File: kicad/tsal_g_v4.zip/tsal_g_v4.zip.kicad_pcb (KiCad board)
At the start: 2 copper layers, 115 x 60 mm, 90 parts, among them J1 Conn_01x02_Pin, J2 Conn_01x02_Pin, J3 Conn_01x06_Pin, J6 Conn_01x02_Pin, J7 Conn_01x02_Pin, J8 Conn_01x03, Q1 2N7002, Q4 QM6015D, U1 TL431DBZ, U10 BU4S01G2, U11 BU4S01G2, U12 4077, U13 BU4S71G2, U14 BUS4S71G2, U16 BU4SU69G2, U2 LTV-817S, U20 4071, U3 B1212, U4 BU4SU69G2, U5 40106, U6 40106, U7 BU4S81G2, U9 40106

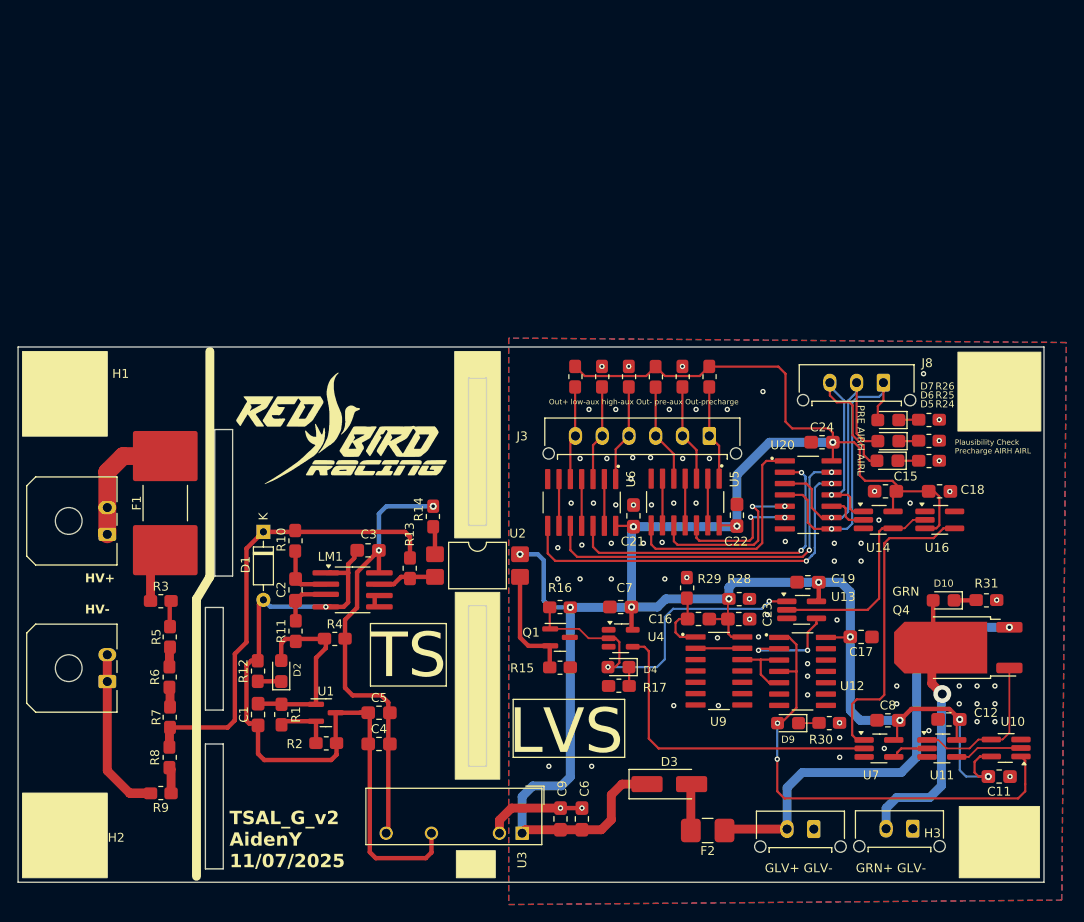
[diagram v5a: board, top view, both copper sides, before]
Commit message: Updated plausibility latch logic
need review
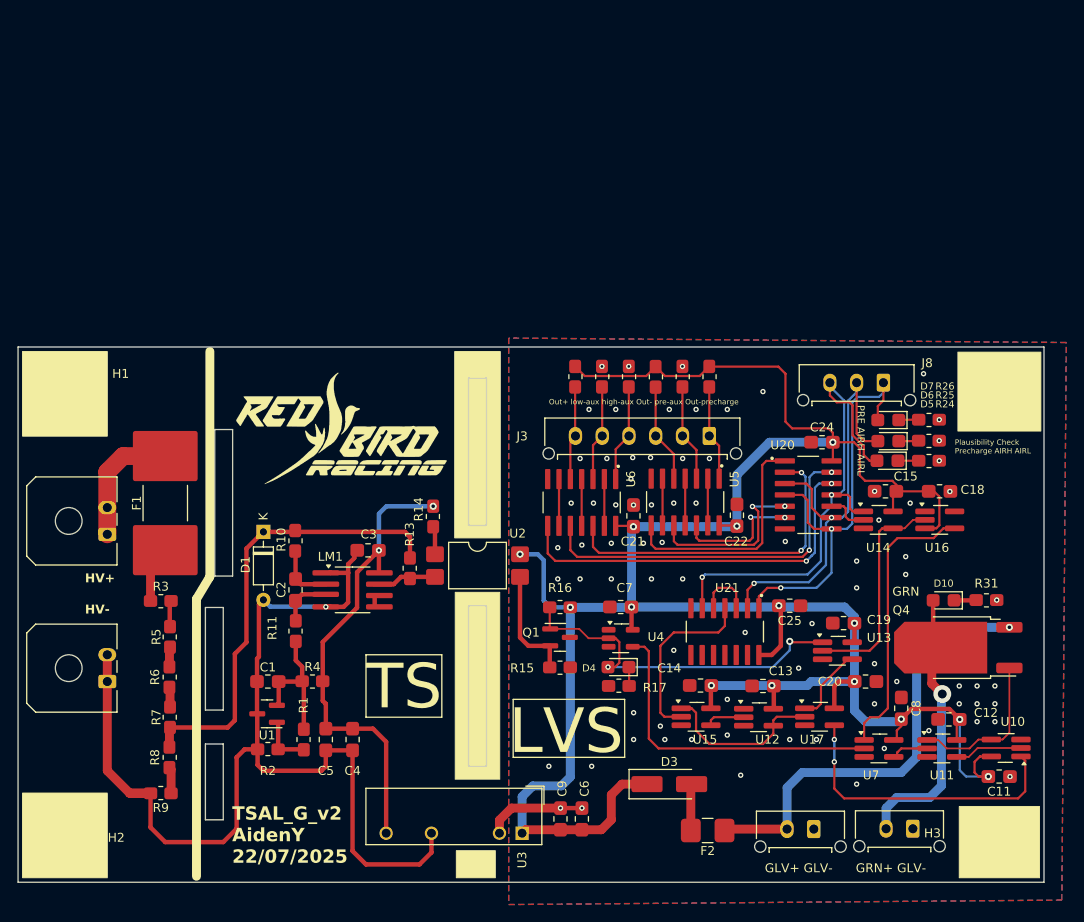
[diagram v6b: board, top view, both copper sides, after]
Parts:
- removed C16, C17, C23: 0.1uF, RMC_Capacitor:C_0805_2012Metric_Pad1.18x1.45mm_HandSolder_L
- removed D2, D9: LED, RMC_LED:LED_0805_2012Metric_Pad1.45x1.40mm_HandSolder
- removed R12, R30: 1k, RMC_Resistor:R_0805_2012Metric_Pad1.20x1.40mm_HandSolder_L
- removed R28: 10k, RMC_Resistor:R_0805_2012Metric_Pad1.20x1.40mm_HandSolder_L
- removed R29: 100k, RMC_Resistor:R_0805_2012Metric_Pad1.20x1.40mm_HandSolder_L
- removed U9: 40106, RMC_SO:SOIC127P600X175-14N
- added C13: 0.1uF, RMC_Capacitor:C_0805_2012Metric_Pad1.18x1.45mm_HandSolder_L, F.Cu at (140.0, 91.0)
- added C14: 0.1uF, RMC_Capacitor:C_0805_2012Metric_Pad1.18x1.45mm_HandSolder_L, F.Cu at (133.0, 91.0)
- added C20: 0.1uF, RMC_Capacitor:C_0805_2012Metric_Pad1.18x1.45mm_HandSolder_L, F.Cu at (151.5, 90.5)
- added C25: 0.1uF, RMC_Capacitor:C_0805_2012Metric_Pad1.18x1.45mm_HandSolder_L, F.Cu at (143.0, 82.0)
- added U15: BU4S01G2, RMC_SOT:SOT-23-5_HandSoldering_Extended_RMC, F.Cu at (132.5, 94.5)
- added U17: BU4S71G2, RMC_SOT:SOT-23-5_HandSoldering_Extended_RMC, F.Cu at (146.3, 94.5)
- added U21: 4071, RMC_SO:SOIC127P600X175-14N, F.Cu at (135.7, 84.9)
- U12: value 4077 -> BU4S01G2; footprint RMC_SO:SOIC127P600X175-14N -> RMC_SOT:SOT-23-5_HandSoldering_Extended_RMC
- moved U12 7.12 mm to (139.5, 94.5)
- moved C5 6.67 mm to (91.0, 97.0), turned to 90 degrees
- moved U1 6.59 mm to (84.4, 94.1), turned to 180 degrees
- moved R2 6.58 mm to (84.5, 98.1), turned to 180 degrees
- moved C19 6.09 mm to (149.0, 84.0)
- moved U13 6.09 mm to (148.3, 87.0)
- moved R4 5.39 mm to (89.5, 90.5)
- moved C1 3.86 mm to (84.5, 90.5), turned to 180 degrees
- moved R1 3.75 mm to (88.5, 97.0)
- moved C4 3.00 mm to (94.0, 97.0), turned to 90 degrees
- moved C8 2.02 mm to (155.5, 93.5), turned to -90 degrees
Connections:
- J2 pad 1: /-HV -> GND
- J2 pad 2: /-HV -> GND
- R9 pad 2: /-HV -> GND
- U1 pad 1: /Vref -> Net-(U1-REF)
- U1 pad 2: Net-(U1-REF) -> /Vref
- U12 pad 1: RESET -> GLV-
- U12 pad 3: Net-(U12-Pad3) -> GLV-
- U12 pad 4: RESET -> Net-(U12-Pad4)
- U12 pad 5: Net-(U12-Pad3) -> VCC
- U13 pad 4: Net-(U12-Pad2) -> Net-(U13-Pad4)
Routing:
- net GND: track 81.7 -> 121.0 mm
- net AIRL Check: track 31.7 -> 57.1 mm, vias 1 -> 2
- net /-HV: track 21.4 -> 0.00 mm
- net RESET: track 54.3 -> 33.4 mm
- net Net-(U15-Pad2): track 0.00 -> 20.2 mm
- net VCC: track 260.5 -> 279.4 mm, vias 12 -> 14
- net Net-(U12-Pad4): track 0.00 -> 18.8 mm
- net AIRH Check: track 34.0 -> 51.0 mm, vias 1 -> 2
- net Precharge Check: track 36.4 -> 49.4 mm, vias 1 -> 2
- net Net-(U13-Pad4): track 0.00 -> 8.77 mm
- net Net-(U12-Pad3): track 8.26 -> 0.00 mm
- net Net-(U12-Pad2): track 11.9 -> 4.38 mm, vias 2 -> 0
- net Net-(C16-Pad2): track 7.35 -> 0.00 mm
- net Net-(U21-Pad3): track 0.00 -> 6.50 mm
- net /Vref: track 21.4 -> 15.6 mm
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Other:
- outline, holes or cut-outs redrawn
- board text added: "TSAL_G_v2 AidenY 22/07/2025"
- board text removed: "TSAL_G_v2 AidenY 11/07/2025"

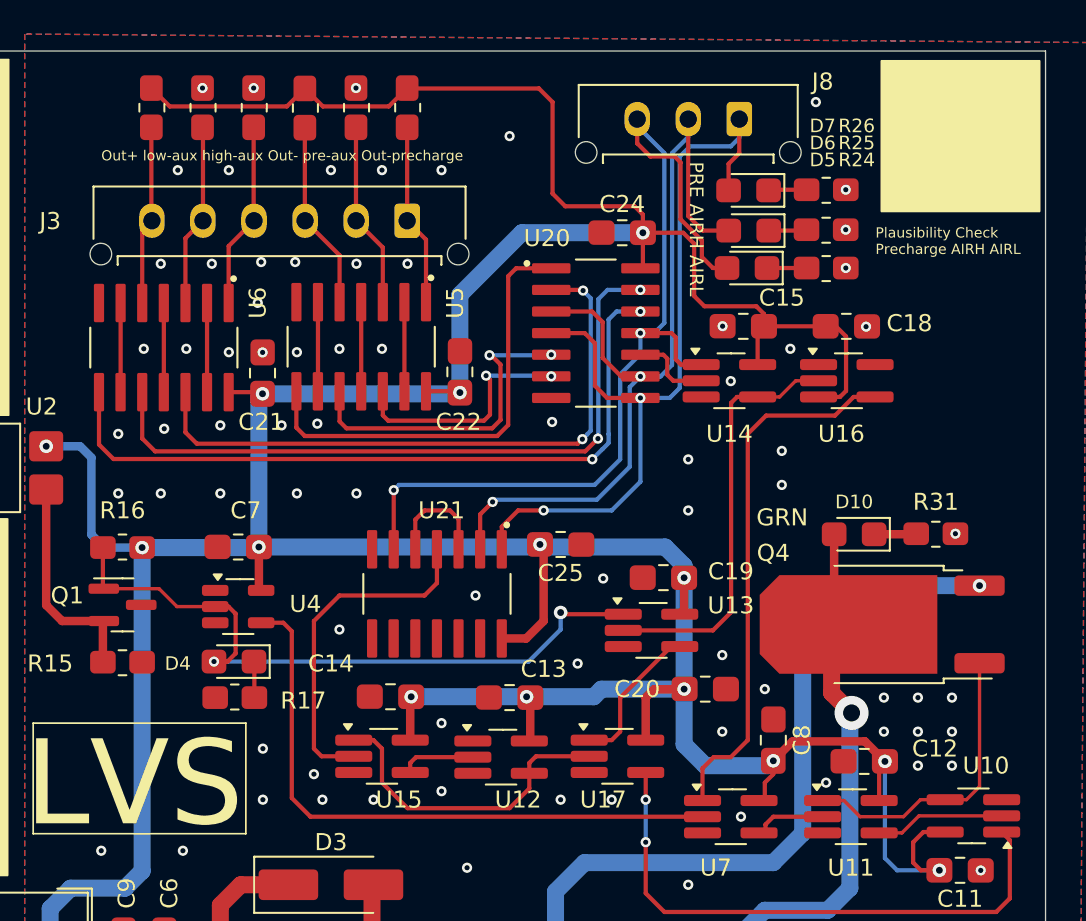
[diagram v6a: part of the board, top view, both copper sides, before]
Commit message: changes in tsal_g
silkscreen, traces
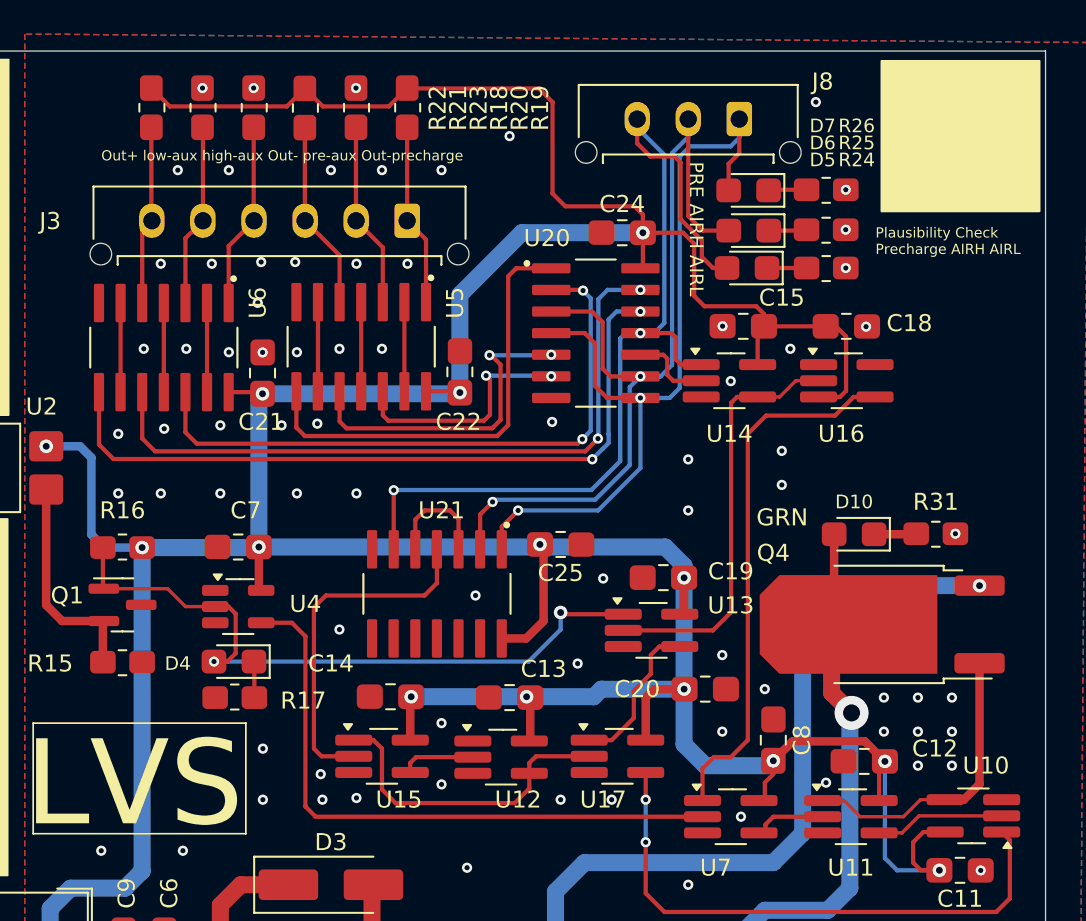
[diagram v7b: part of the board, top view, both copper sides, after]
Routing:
- net AIRL Check: track 57.1 -> 57.7 mm

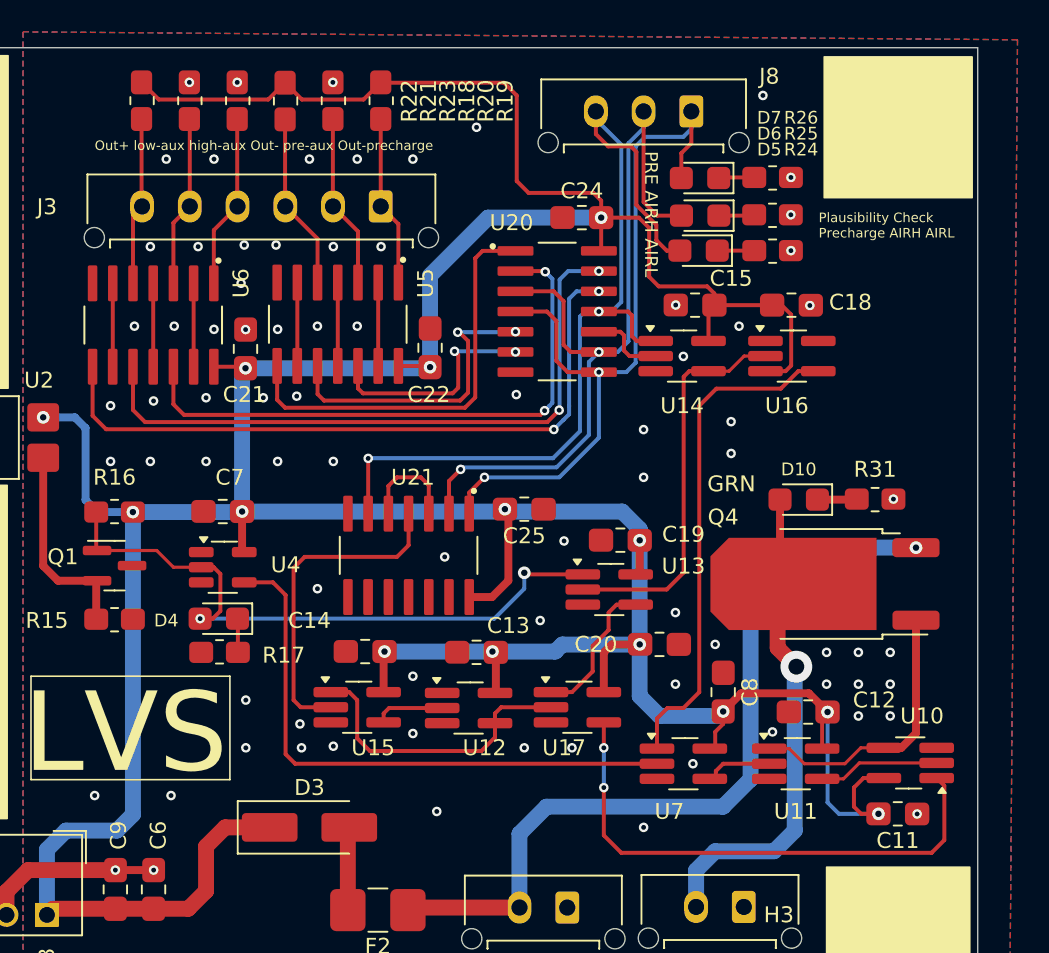
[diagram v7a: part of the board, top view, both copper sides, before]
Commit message: updated cd4001
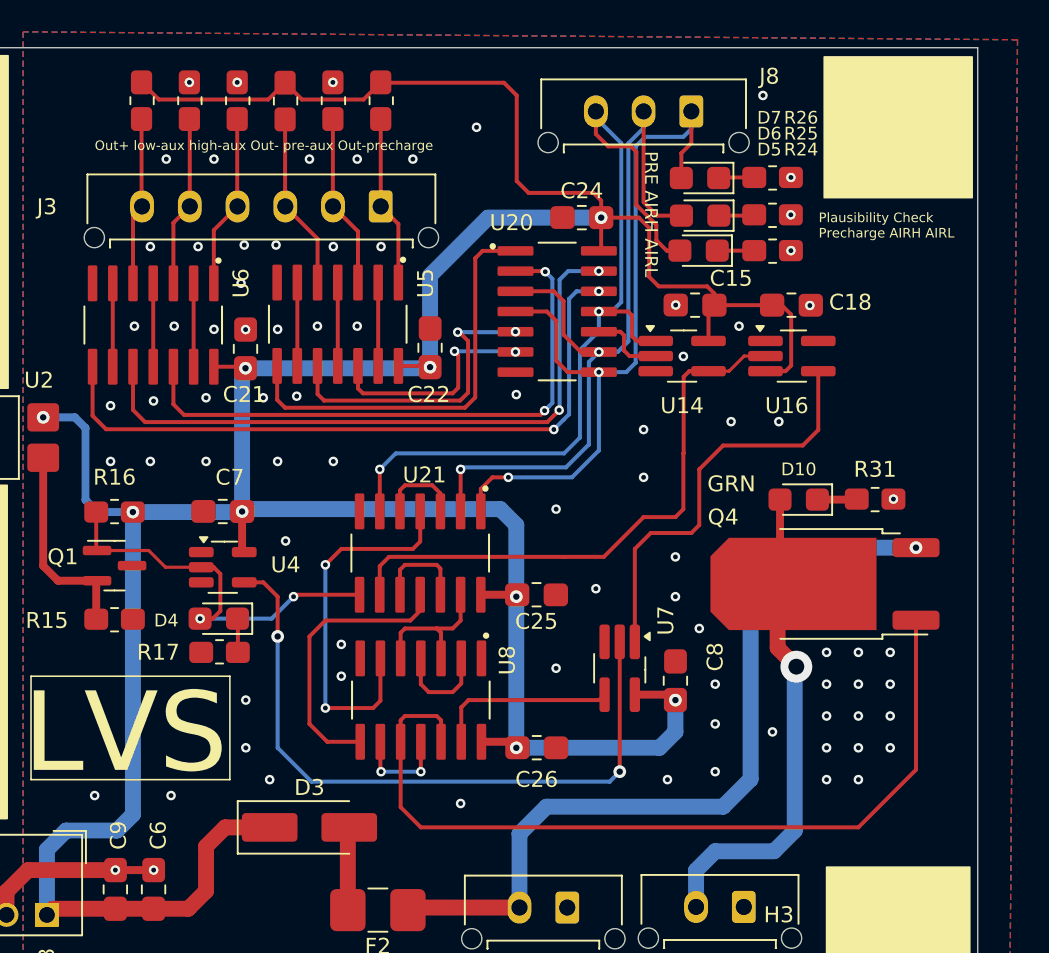
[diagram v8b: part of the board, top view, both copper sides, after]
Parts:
- removed C11, C12, C13, C14, C19, C20: 0.1uF, RMC_Capacitor:C_0805_2012Metric_Pad1.18x1.45mm_HandSolder_L
- removed U10, U11, U12, U15: BU4S01G2, RMC_SOT:SOT-23-5_HandSoldering_Extended_RMC
- removed U13, U17: BU4S71G2, RMC_SOT:SOT-23-5_HandSoldering_Extended_RMC
- added C26: 0.1uF, RMC_Capacitor:C_0805_2012Metric_Pad1.18x1.45mm_HandSolder_L, F.Cu at (143.8, 97.0)
- added U8: 4001, RMC_SO:SOIC127P600X175-14N, F.Cu at (136.5, 94.0)
- moved U7 7.21 mm to (149.0, 92.0), turned to -90 degrees
- moved C25 5.43 mm to (143.8, 87.4)
- moved C8 3.08 mm to (152.5, 92.8)
- moved U21 0.74 mm to (136.5, 84.8)
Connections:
- U21 pad 10: unconnected-(U21-Pad10) -> Net-(U21-Pad10)
- U21 pad 11: unconnected-(U21-Pad11) -> RESET
- U21 pad 12: unconnected-(U21-Pad12) -> Net-(U21-Pad10)
- U21 pad 13: unconnected-(U21-Pad13) -> Net-(U21-Pad13)
- U21 pad 8: unconnected-(U21-Pad8) -> TS RESET
- U21 pad 9: unconnected-(U21-Pad9) -> RELAY RESET
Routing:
- net VCC: track 279.4 -> 226.0 mm, vias 14 -> 9
- net Net-(Q4-G): track 17.5 -> 53.4 mm
- net Net-(U12-Pad4): track 18.8 -> 0.00 mm
- net RESET: track 33.4 -> 17.8 mm, vias 2 -> 0
- net TS RESET: track 40.5 -> 25.2 mm
- net RELAY RESET: track 24.8 -> 36.4 mm
- net Net-(U21-Pad13): track 0.00 -> 9.31 mm
- net Net-(U13-Pad4): track 9.18 -> 0.00 mm
- net Net-(U10-Pad2): track 7.61 -> 0.00 mm
- net Net-(U7-Pad4): track 4.04 -> 11.5 mm
- net Net-(U8-Pad11): track 0.00 -> 6.28 mm, vias 0 -> 2
- net Net-(U8-Pad2): track 0.00 -> 6.17 mm
- net Net-(U21-Pad10): track 0.00 -> 5.98 mm
- net TS LOGIC: track 36.9 -> 42.8 mm, vias 0 -> 2
- net RELAY LOGIC: track 31.6 -> 26.2 mm
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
